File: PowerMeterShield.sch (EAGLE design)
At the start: 33 parts, among them U1 INA170EA/2K5, U2 THS4521, U3 INA138, U4 ADUM1250ARZ, U5 MCP3426A0-E/SN, U6 ISL21080

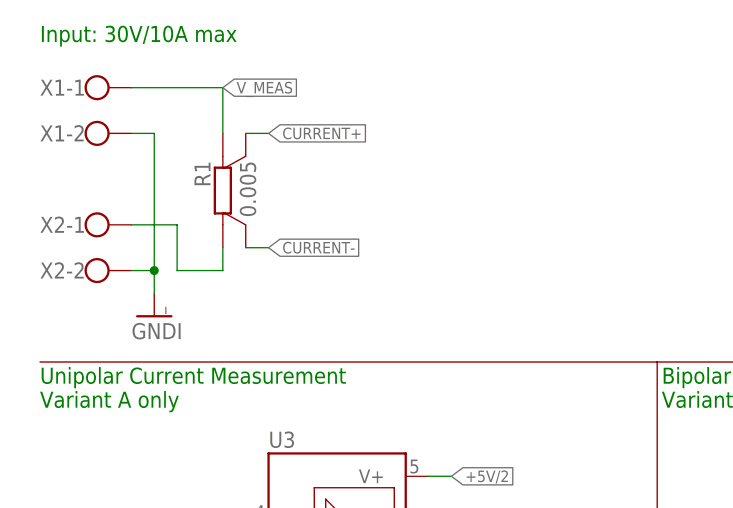
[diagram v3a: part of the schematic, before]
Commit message: Fixed fuse designator, misc silkscreen fixes
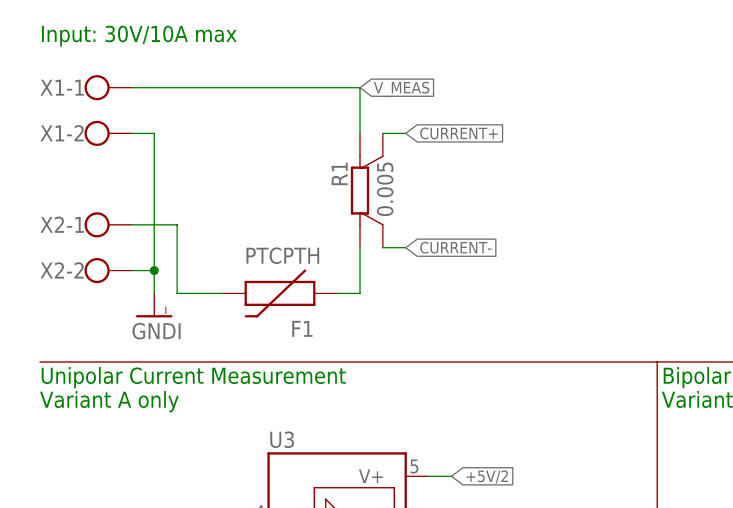
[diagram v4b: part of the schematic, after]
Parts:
- added F1: PTCPTH, SparkFun:PTCPTH
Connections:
- new net N$3: F1.1, R1.I1
- net VIN_MEAS: now also F1.2; no longer R1.I1
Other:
- moved on the sheet: R1
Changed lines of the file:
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@@
 <part name="R22" library="rcl" deviceset="R-EU_" device="R2010" value="0"/>
 <part name="R23" library="rcl" deviceset="R-EU_" device="R2010" value="0"/>
+<part name="F1" library="SparkFun" deviceset="PTC" device="PTH">
+<attribute name="OC_DIGIKEY" value="RGEF1000-ND"/>
+<attribute name="PRICE_10" value="0.59"/>
+</part>
 </parts>
 <sheets>
@@
 </plain>
 <instances>
-<instance part="R1" gate="G$1" x="25.4" y="154.94" smashed="yes" rot="MR270">
-<attribute name="OC_FARNELL" x="25.4" y="154.94" size="1.27" layer="96" rot="MR270" display="off"/>
-<attribute name="PRICE_10" x="25.4" y="154.94" size="1.27" layer="96" rot="MR270" display="off"/>
-<attribute name="NAME" x="24.0284" y="159.512" size="1.778" layer="95" rot="MR270"/>
-<attribute name="VALUE" x="29.083" y="159.512" size="1.778" layer="96" rot="MR270"/>
+<instance part="R1" gate="G$1" x="40.64" y="154.94" smashed="yes" rot="MR270">
+<attribute name="OC_FARNELL" x="40.64" y="154.94" size="1.27" layer="96" rot="MR270" display="off"/>
+<attribute name="PRICE_10" x="40.64" y="154.94" size="1.27" layer="96" rot="MR270" display="off"/>
+<attribute name="NAME" x="39.2684" y="159.512" size="1.778" layer="95" rot="MR270"/>
+<attribute name="VALUE" x="44.323" y="159.512" size="1.778" layer="96" rot="MR270"/>
 </instance>
 <instance part="GND1" gate="G$1" x="17.78" y="142.24"/>
@@
 <instance part="R22" gate="G$1" x="38.1" y="40.64"/>
 <instance part="R23" gate="G$1" x="38.1" y="33.02"/>
+<instance part="F1" gate="G$1" x="33.02" y="144.78" rot="R180">
+<attribute name="PRICE_10" x="33.02" y="144.78" size="1.778" layer="96" rot="R180" display="off"/>
+<attribute name="OC_DIGIKEY" x="33.02" y="144.78" size="1.778" layer="96" rot="R180" display="off"/>
+</instance>
 </instances>
 <busses>
@@
 <net name="VIN_MEAS" class="1">
 <segment>
-<wire x1="20.32" y1="152.4" x2="20.32" y2="147.32" width="0.1524" layer="91"/>
-<wire x1="20.32" y1="147.32" x2="25.4" y2="147.32" width="0.1524" layer="91"/>
+<wire x1="20.32" y1="152.4" x2="20.32" y2="144.78" width="0.1524" layer="91"/>
+<wire x1="20.32" y1="144.78" x2="25.4" y2="144.78" width="0.1524" layer="91"/>
 <wire x1="15.24" y1="152.4" x2="20.32" y2="152.4" width="0.1524" layer="91"/>
 <pinref part="X2" gate="-1" pin="KL"/>
-<pinref part="R1" gate="G$1" pin="I1"/>
-<wire x1="25.4" y1="147.32" x2="25.4" y2="149.86" width="0.1524" layer="91"/>
+<pinref part="F1" gate="G$1" pin="2"/>
 </segment>
 </net>
 <net name="V_MEAS" class="1">
 <segment>
-<wire x1="25.4" y1="167.64" x2="15.24" y2="167.64" width="0.1524" layer="91"/>
+<wire x1="40.64" y1="167.64" x2="15.24" y2="167.64" width="0.1524" layer="91"/>
 <pinref part="X1" gate="-1" pin="KL"/>
 <pinref part="R1" gate="G$1" pin="I2"/>
-<wire x1="25.4" y1="162.56" x2="25.4" y2="167.64" width="0.1524" layer="91"/>
-<label x="25.4" y="167.64" size="1.27" layer="95" xref="yes"/>
+<wire x1="40.64" y1="162.56" x2="40.64" y2="167.64" width="0.1524" layer="91"/>
+<label x="40.64" y="167.64" size="1.27" layer="95" xref="yes"/>
 </segment>
 <segment>
@@
 <segment>
 <pinref part="R1" gate="G$1" pin="S2"/>
-<wire x1="30.48" y1="162.56" x2="27.94" y2="162.56" width="0.1524" layer="91"/>
-<label x="30.48" y="162.56" size="1.27" layer="95" xref="yes"/>
+<wire x1="45.72" y1="162.56" x2="43.18" y2="162.56" width="0.1524" layer="91"/>
+<label x="45.72" y="162.56" size="1.27" layer="95" xref="yes"/>
 </segment>
 <segment>
@@
 <segment>
 <pinref part="R1" gate="G$1" pin="S1"/>
-<wire x1="30.48" y1="149.86" x2="27.94" y2="149.86" width="0.1524" layer="91"/>
-<label x="30.48" y="149.86" size="1.27" layer="95" xref="yes"/>
+<wire x1="45.72" y1="149.86" x2="43.18" y2="149.86" width="0.1524" layer="91"/>
+<label x="45.72" y="149.86" size="1.27" layer="95" xref="yes"/>
 </segment>
 <segment>
@@
 </segment>
 </net>
+<net name="N$3" class="0">
+<segment>
+<pinref part="R1" gate="G$1" pin="I1"/>
+<wire x1="40.64" y1="149.86" x2="40.64" y2="144.78" width="0.1524" layer="91"/>
+<pinref part="F1" gate="G$1" pin="1"/>
+<wire x1="40.64" y1="144.78" x2="38.1" y2="144.78" width="0.1524" layer="91"/>
+</segment>
+</net>

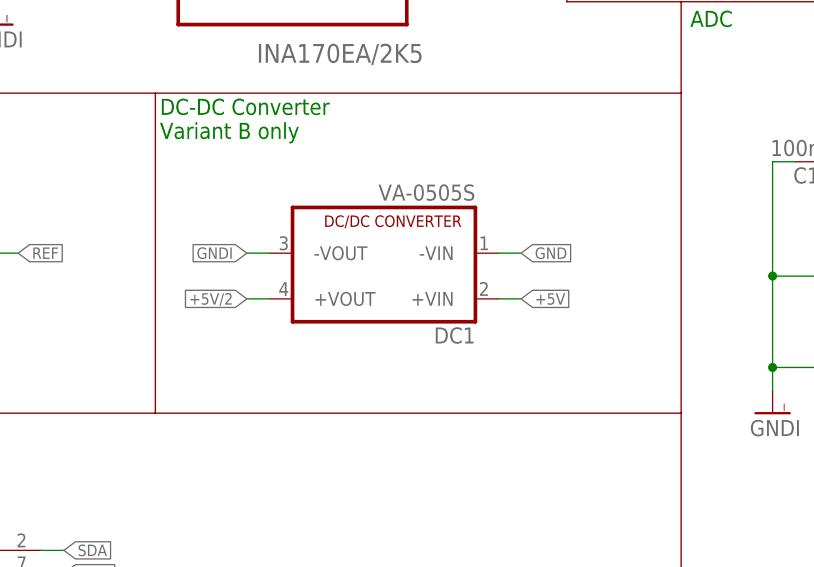
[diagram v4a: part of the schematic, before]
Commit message: Added SMD DC-DC converter to match height of the shield headers (old one was 10mm high, new one is only 6.3mm high) Added silkscreen for the arduino headers
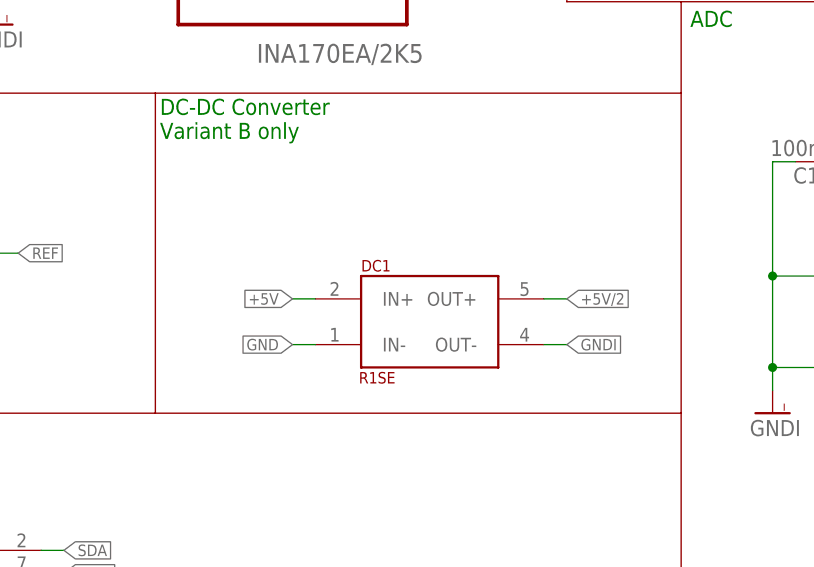
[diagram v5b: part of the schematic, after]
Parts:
- DC1: value VA-0505S -> R1SE; device dc-dc-converter:VA-0505S -> R1SE:R1SE; OC_FARNELL 2079696 -> (none)
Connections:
- net +5V: now also DC1.IN+; no longer DC1.+VIN
- net +5V/2: now also DC1.OUT+; no longer DC1.+VOUT
- net GND: now also DC1.IN-; no longer DC1.-VIN
- net GNDI: now also DC1.OUT-; no longer DC1.-VOUT
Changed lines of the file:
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@@
 <attribute name="PRICE_100" value="0.005"/>
-</part>
-<part name="DC1" library="dc-dc-converter" deviceset="VA-*?" device="S" technology="0505" value="VA-0505S">
-<attribute name="OC_FARNELL" value="2079696"/>
 </part>
 <part name="U4" library="Adum1250" deviceset="ADUM1250ARZ" device=""/>
@@
 <attribute name="PRICE_10" value="0.59"/>
 </part>
+<part name="DC1" library="R1SE" deviceset="R1SE" device=""/>
 </parts>
 <sheets>
@@
 <attribute name="OC_FARNELL" x="195.58" y="76.2" size="1.27" layer="96" rot="R270" display="off"/>
 </instance>
-<instance part="DC1" gate="G$1" x="144.78" y="63.5" rot="R180"/>
 <instance part="U4" gate="A" x="88.9" y="27.94"/>
 <instance part="FRAME1" gate="G$1" x="0" y="0"/>
@@
 <attribute name="OC_DIGIKEY" x="33.02" y="144.78" size="1.778" layer="96" rot="R180" display="off"/>
 </instance>
+<instance part="DC1" gate="G$1" x="149.86" y="58.42"/>
 </instances>
 <busses>
@@
 </segment>
 <segment>
-<pinref part="DC1" gate="G$1" pin="-VIN"/>
-<wire x1="157.48" y1="66.04" x2="160.02" y2="66.04" width="0.1524" layer="91"/>
-<label x="160.02" y="66.04" size="1.27" layer="95" xref="yes"/>
+<wire x1="137.16" y1="55.88" x2="134.62" y2="55.88" width="0.1524" layer="91"/>
+<label x="134.62" y="55.88" size="1.27" layer="95" rot="R180" xref="yes"/>
+<pinref part="DC1" gate="G$1" pin="IN-"/>
 </segment>
 <segment>
@@
 </segment>
 <segment>
-<pinref part="DC1" gate="G$1" pin="+VIN"/>
-<wire x1="157.48" y1="60.96" x2="160.02" y2="60.96" width="0.1524" layer="91"/>
-<label x="160.02" y="60.96" size="1.27" layer="95" xref="yes"/>
+<wire x1="137.16" y1="60.96" x2="134.62" y2="60.96" width="0.1524" layer="91"/>
+<label x="134.62" y="60.96" size="1.27" layer="95" rot="R180" xref="yes"/>
+<pinref part="DC1" gate="G$1" pin="IN+"/>
 </segment>
 <segment>
@@
 <net name="GNDI" class="0">
 <segment>
-<pinref part="DC1" gate="G$1" pin="-VOUT"/>
-<wire x1="132.08" y1="66.04" x2="129.54" y2="66.04" width="0.1524" layer="91"/>
-<label x="129.54" y="66.04" size="1.27" layer="95" rot="R180" xref="yes"/>
+<wire x1="162.56" y1="55.88" x2="165.1" y2="55.88" width="0.1524" layer="91"/>
+<label x="165.1" y="55.88" size="1.27" layer="95" xref="yes"/>
+<pinref part="DC1" gate="G$1" pin="OUT-"/>
 </segment>
 <segment>
@@
 <net name="+5V/2" class="0">
 <segment>
-<pinref part="DC1" gate="G$1" pin="+VOUT"/>
-<wire x1="132.08" y1="60.96" x2="129.54" y2="60.96" width="0.1524" layer="91"/>
-<label x="129.54" y="60.96" size="1.27" layer="95" rot="R180" xref="yes"/>
-</segment>
-<segment>
+<wire x1="162.56" y1="60.96" x2="165.1" y2="60.96" width="0.1524" layer="91"/>
+<label x="165.1" y="60.96" size="1.27" layer="95" xref="yes"/>
+<pinref part="DC1" gate="G$1" pin="OUT+"/>
+</segment>
+<segment>
